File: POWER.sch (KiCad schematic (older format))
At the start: 58 parts

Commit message: update power mark,
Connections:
- net labels added: VCC-IO
- net labels removed: Vcc-io
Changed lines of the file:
@@
 $Descr A3 16535 11693
 encoding utf-8
-Sheet 6 33
+Sheet 6 34
 Title ""
 Date ""
@@
 $EndComp
 $Comp
-L taobao-components:Vcc-io #PWR?
-U 1 1 5C34B9F1
-P 10800 4400
-F 0 "#PWR?" H 10800 4250 50  0001 C CNN
-F 1 "Vcc-io" H 10850 4550 50  0000 C CNN
-F 2 "" H 10800 4400 50  0001 C CNN
-F 3 "" H 10800 4400 50  0001 C CNN
-	1    10800 4400
-	1    0    0    -1
-$EndComp
-$Comp
 L taobao-c:C104,0603 C?
 U 1 1 5C34BB9C
@@
 Wire Wire Line
 	8550 4800 8550 5200
-$Comp
-L taobao-components:Vcc-io #PWR?
-U 1 1 5C39DCD8
-P 8550 6050
-F 0 "#PWR?" H 8550 5900 50  0001 C CNN
-F 1 "Vcc-io" H 8600 6200 50  0000 C CNN
-F 2 "" H 8550 6050 50  0001 C CNN
-F 3 "" H 8550 6050 50  0001 C CNN
-	1    8550 6050
-	1    0    0    -1
-$EndComp
 $Comp
 L taobao-components:AVCC #PWR?
@@
 Wire Wire Line
 	9550 6200 10100 6200
+$Comp
+L taobao-components:VCC-IO #PWR?
+U 1 1 5C7D7758
+P 10800 4400
+F 0 "#PWR?" H 10800 4250 50  0001 C CNN
+F 1 "VCC-IO" H 10850 4550 50  0000 C CNN
+F 2 "" H 10800 4400 50  0001 C CNN
+F 3 "" H 10800 4400 50  0001 C CNN
+	1    10800 4400
+	1    0    0    -1
+$EndComp
+$Comp
+L taobao-components:VCC-IO #PWR?
+U 1 1 5C7D78DC
+P 8550 6050
+F 0 "#PWR?" H 8550 5900 50  0001 C CNN
+F 1 "VCC-IO" H 8600 6200 50  0000 C CNN
+F 2 "" H 8550 6050 50  0001 C CNN
+F 3 "" H 8550 6050 50  0001 C CNN
+	1    8550 6050
+	1    0    0    -1
+$EndComp
 $EndSCHEMATC

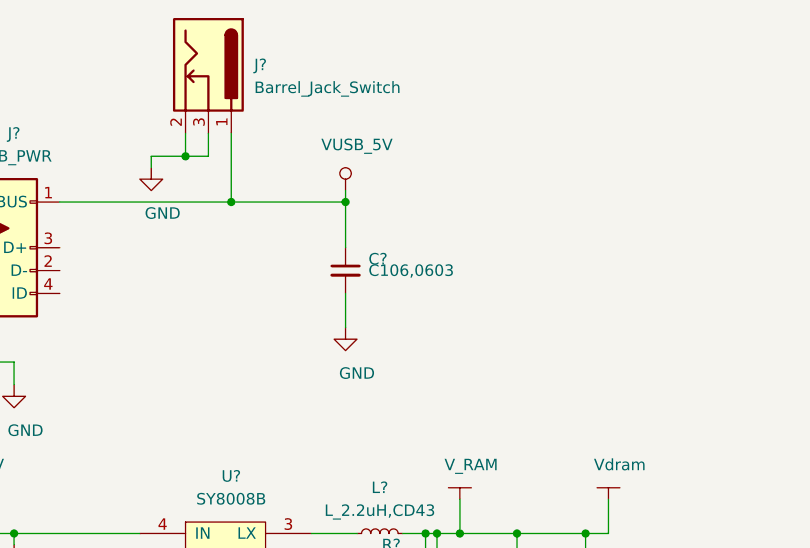
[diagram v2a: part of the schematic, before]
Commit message: add fuse,
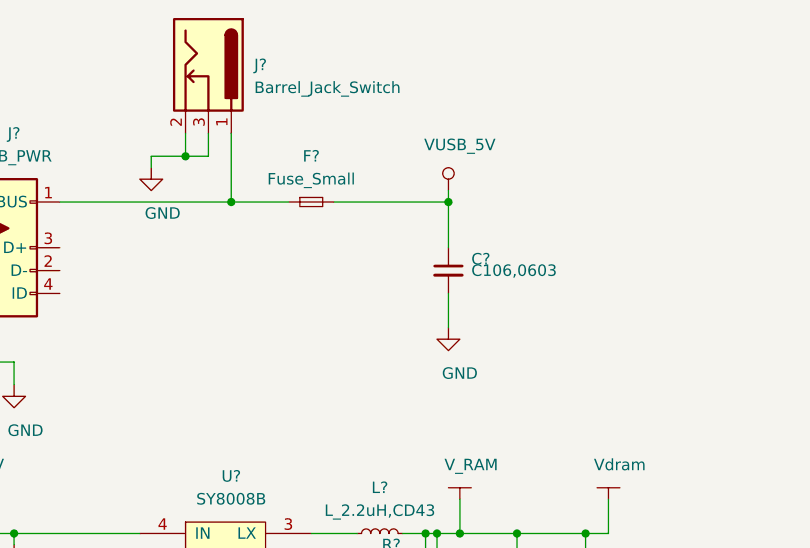
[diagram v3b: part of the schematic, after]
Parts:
- added F?: Fuse_Small, symbol Device:Fuse_Small
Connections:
- net VUSB_5V: now also F?.2; no longer J?.1, J?.1 (VBUS)
- new net: F?.1, J?.1, J?.1 (VBUS)
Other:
- moved on the sheet: C?
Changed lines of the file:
@@
 L taobao-components:VUSB_5V #PWR?
 U 1 1 5C785224
-P 5900 2000
-F 0 "#PWR?" H 5900 1850 50  0001 C CNN
-F 1 "VUSB_5V" H 5950 2200 50  0000 C CNN
-F 2 "" H 5900 2000 50  0001 C CNN
-F 3 "" H 5900 2000 50  0001 C CNN
-	1    5900 2000
+P 6350 2000
+F 0 "#PWR?" H 6350 1850 50  0001 C CNN
+F 1 "VUSB_5V" H 6400 2200 50  0000 C CNN
+F 2 "" H 6350 2000 50  0001 C CNN
+F 3 "" H 6350 2000 50  0001 C CNN
+	1    6350 2000
 	1    0    0    -1
 $EndComp
@@
 L taobao-c:C106,0603 C?
 U 1 1 5C7853BF
-P 5900 2350
-F 0 "C?" H 6000 2400 50  0000 L CNN
-F 1 "C106,0603" H 6000 2350 50  0000 L CNN
-F 2 "Capacitor_SMD:C_0603_1608Metric_Pad1.05x0.95mm_HandSolder" H 5900 2350 50  0001 C CNN
-F 3 "~" H 5900 2350 50  0001 C CNN
-	1    5900 2350
-	1    0    0    -1
-$EndComp
-Wire Wire Line
-	5400 2050 5900 2050
-Wire Wire Line
-	5900 2050 5900 2000
-Connection ~ 5400 2050
-Wire Wire Line
-	5900 2050 5900 2250
-Connection ~ 5900 2050
+P 6350 2350
+F 0 "C?" H 6450 2400 50  0000 L CNN
+F 1 "C106,0603" H 6450 2350 50  0000 L CNN
+F 2 "Capacitor_SMD:C_0603_1608Metric_Pad1.05x0.95mm_HandSolder" H 6350 2350 50  0001 C CNN
+F 3 "~" H 6350 2350 50  0001 C CNN
+	1    6350 2350
+	1    0    0    -1
+$EndComp
+Wire Wire Line
+	6350 2050 6350 2000
+Wire Wire Line
+	6350 2050 6350 2250
+Connection ~ 6350 2050
 $Comp
 L power:GND #PWR?
 U 1 1 5C78561A
-P 5900 2600
-F 0 "#PWR?" H 5900 2350 50  0001 C CNN
-F 1 "GND" H 5950 2400 50  0000 C CNN
-F 2 "" H 5900 2600 50  0001 C CNN
-F 3 "" H 5900 2600 50  0001 C CNN
-	1    5900 2600
-	1    0    0    -1
-$EndComp
-Wire Wire Line
-	5900 2450 5900 2600
+P 6350 2600
+F 0 "#PWR?" H 6350 2350 50  0001 C CNN
+F 1 "GND" H 6400 2400 50  0000 C CNN
+F 2 "" H 6350 2600 50  0001 C CNN
+F 3 "" H 6350 2600 50  0001 C CNN
+	1    6350 2600
+	1    0    0    -1
+$EndComp
+Wire Wire Line
+	6350 2450 6350 2600
 $Comp
 L taobao-components:VUSB_5V #PWR?
@@
 	1    0    0    -1
 $EndComp
+$Comp
+L Device:Fuse_Small F?
+U 1 1 5C37F30E
+P 5750 2050
+F 0 "F?" H 5750 2250 50  0000 C CNN
+F 1 "Fuse_Small" H 5750 2150 50  0000 C CNN
+F 2 "" H 5750 2050 50  0001 C CNN
+F 3 "~" H 5750 2050 50  0001 C CNN
+	1    5750 2050
+	1    0    0    -1
+$EndComp
+Wire Wire Line
+	5650 2050 5400 2050
+Connection ~ 5400 2050
+Wire Wire Line
+	5850 2050 6350 2050
 $EndSCHEMATC

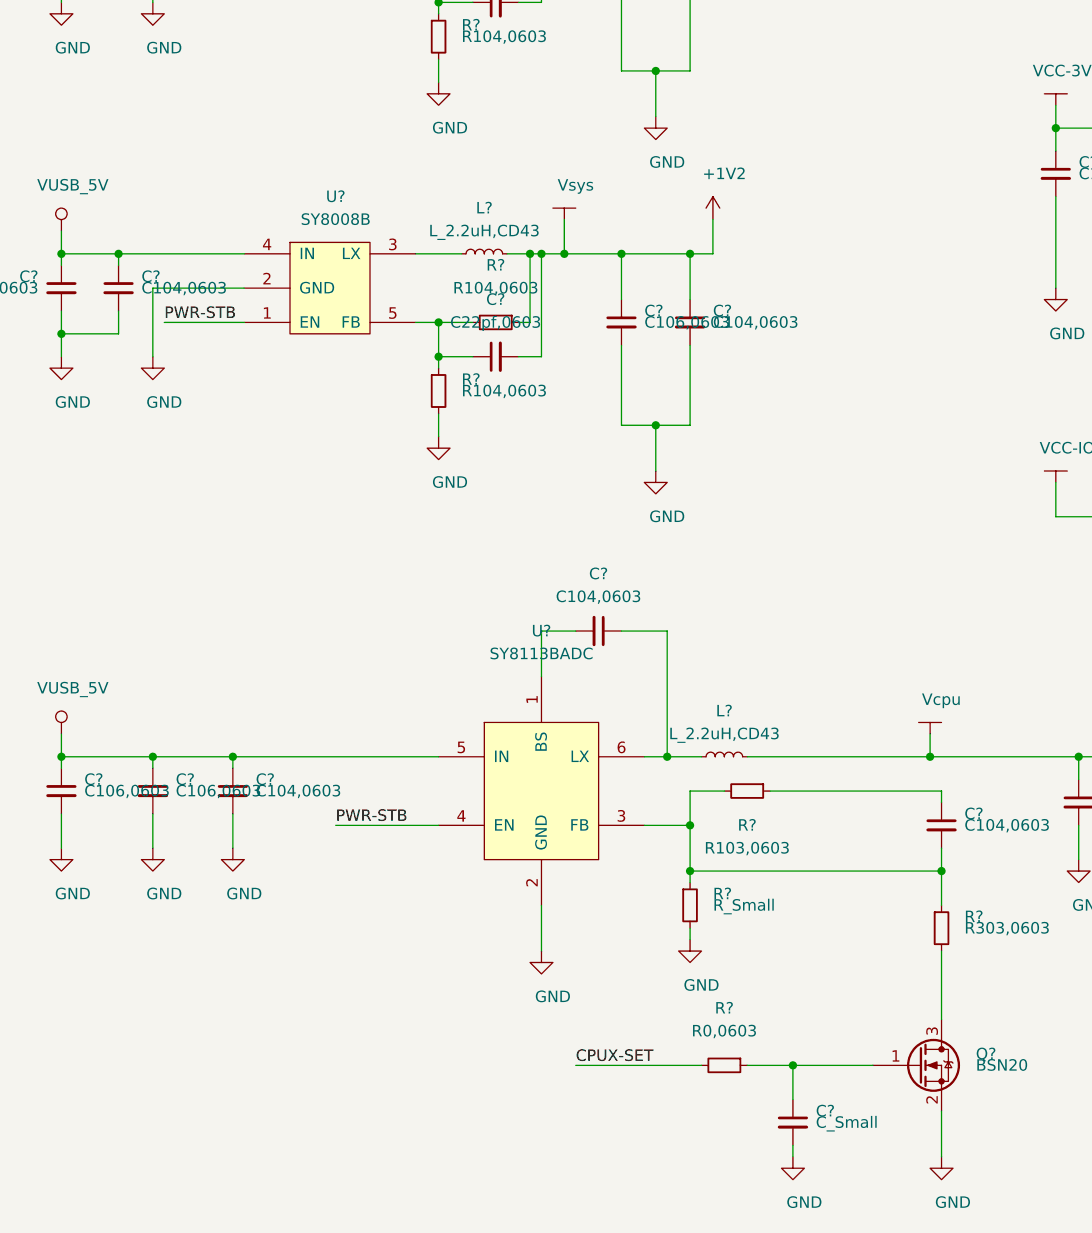
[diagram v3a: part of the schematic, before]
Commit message: update CPU power,
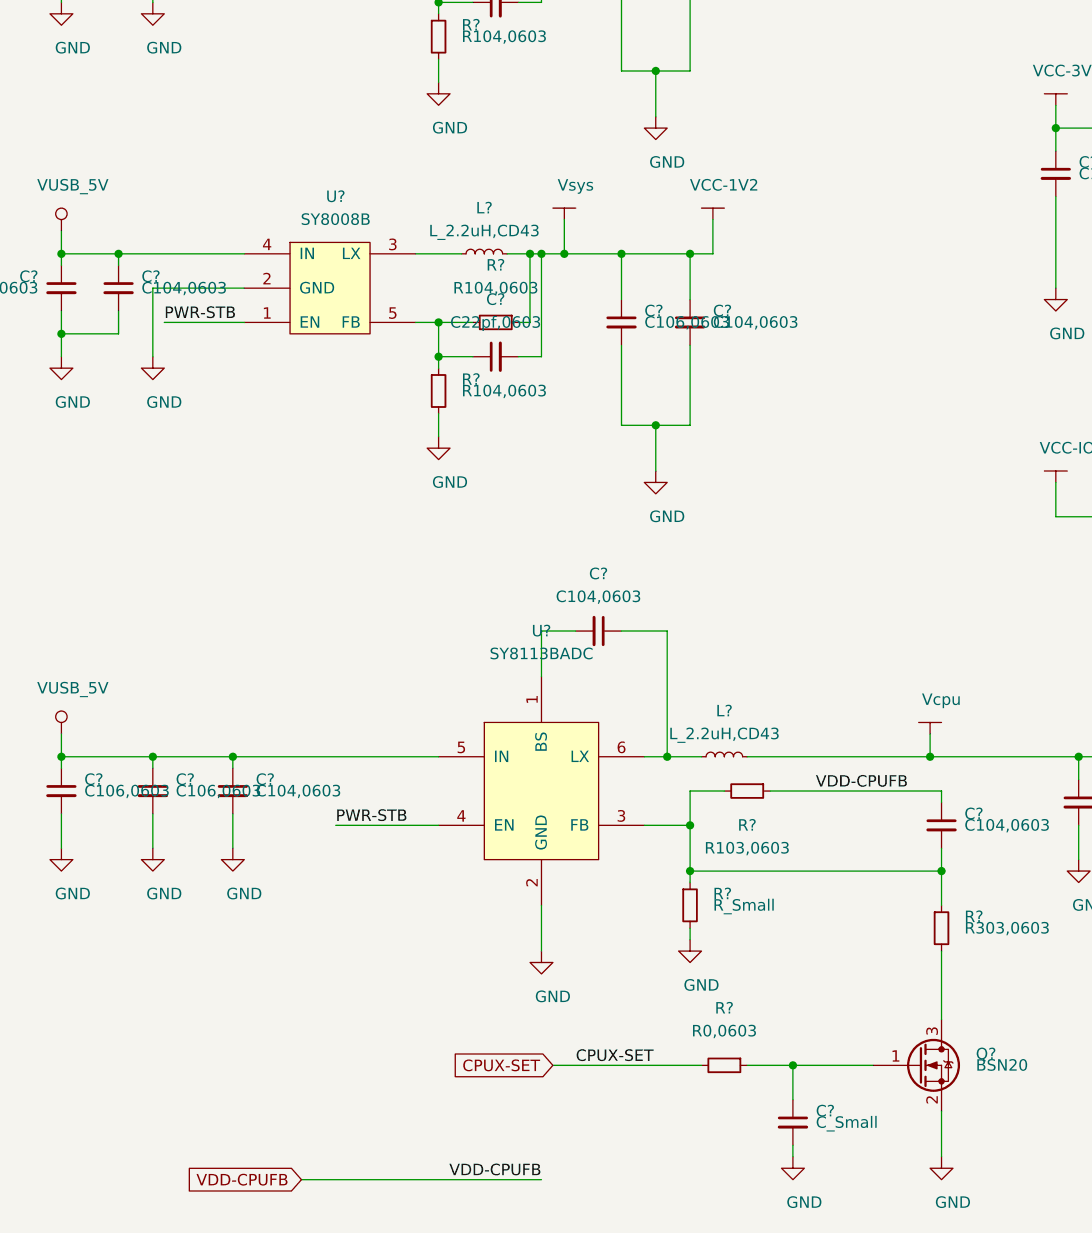
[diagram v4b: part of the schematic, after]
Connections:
- net VDD-CPUFB: now reaches C?.1, R?.1
- net +1V2 renamed VCC-1V2
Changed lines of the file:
@@
-$EndComp
-$Comp
-L power:+1V2 #PWR?
-U 1 1 5C1E907F
-P 7050 4900
-F 0 "#PWR?" H 7050 4750 50  0001 C CNN
-F 1 "+1V2" H 7100 5100 50  0000 C CNN
-F 2 "" H 7050 4900 50  0001 C CNN
-F 3 "" H 7050 4900 50  0001 C CNN
-	1    7050 4900
-	1    0    0    -1
 $EndComp
 $Comp
@@
 Text Label 6450 8600 0    50   ~ 0
 CPUX-SET
-Wire Wire Line
-	6450 8600 7000 8600
 $Comp
 L taobao-components:VUSB_5V #PWR?
@@
 Wire Wire Line
 	5850 2050 6350 2050
+$Comp
+L taobao-components:VCC-1V2 #PWR?
+U 1 1 5C3A3C4D
+P 7050 4900
+F 0 "#PWR?" H 7050 4750 50  0001 C CNN
+F 1 "VCC-1V2" H 7100 5050 50  0000 C CNN
+F 2 "" H 7050 4900 50  0001 C CNN
+F 3 "" H 7050 4900 50  0001 C CNN
+	1    7050 4900
+	1    0    0    -1
+$EndComp
+Text Label 7500 7400 0    50   ~ 0
+VDD-CPUFB
+Text Label 6300 9100 2    50   ~ 0
+VDD-CPUFB
+Text GLabel 5250 9100 0    50   Input ~ 0
+VDD-CPUFB
+Wire Wire Line
+	5250 9100 6300 9100
+Wire Wire Line
+	6350 8600 7000 8600
+Text GLabel 6350 8600 0    50   Input ~ 0
+CPUX-SET
 $EndSCHEMATC

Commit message: update,
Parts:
- removed C?: C104,0603, Capacitor_SMD:C_0603_1608Metric_Pad1.05x0.95mm_HandSolder, symbol taobao-c:C104,0603
- added C?: C_NC,0603, Capacitor_SMD:C_0603_1608Metric_Pad1.05x0.95mm_HandSolder, symbol taobao-components:C_NC,0603
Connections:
- net VDD-CPUFB: now also C?.1
- net at R?.1, R?.1, R?.2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: now also C?.2
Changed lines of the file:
@@
 P 4200 7400
 F 0 "C?" H 4300 7450 50  0000 L CNN
-F 1 "C106,0603" H 4300 7400 50  0000 L CNN
+F 1 "C106,0603" V 4300 7400 50  0000 L CNN
 F 2 "Capacitor_SMD:C_0603_1608Metric_Pad1.05x0.95mm_HandSolder" H 4200 7400 50  0001 C CNN
 F 3 "~" H 4200 7400 50  0001 C CNN
@@
 P 4600 7400
 F 0 "C?" H 4700 7450 50  0000 L CNN
-F 1 "C106,0603" H 4700 7400 50  0000 L CNN
+F 1 "C106,0603" V 4700 7400 50  0000 L CNN
 F 2 "Capacitor_SMD:C_0603_1608Metric_Pad1.05x0.95mm_HandSolder" H 4600 7400 50  0001 C CNN
 F 3 "~" H 4600 7400 50  0001 C CNN
@@
 P 4950 7400
 F 0 "C?" H 5050 7450 50  0000 L CNN
-F 1 "C104,0603" H 5050 7400 50  0000 L CNN
+F 1 "C104,0603" V 5050 7400 50  0000 L CNN
 F 2 "Capacitor_SMD:C_0603_1608Metric_Pad1.05x0.95mm_HandSolder" H 4950 7400 50  0001 C CNN
 F 3 "~" H 4950 7400 50  0001 C CNN
@@
 	6950 7400 6950 7550
 Connection ~ 6950 7550
-$Comp
-L taobao-c:C104,0603 C?
-U 1 1 5C2268D4
-P 8050 7550
-F 0 "C?" H 8150 7600 50  0000 L CNN
-F 1 "C104,0603" H 8150 7550 50  0000 L CNN
-F 2 "Capacitor_SMD:C_0603_1608Metric_Pad1.05x0.95mm_HandSolder" H 8050 7550 50  0001 C CNN
-F 3 "~" H 8050 7550 50  0001 C CNN
-	1    8050 7550
-	1    0    0    -1
-$EndComp
 Wire Wire Line
 	8050 7450 8050 7400
@@
 P 8650 7450
 F 0 "C?" H 8750 7500 50  0000 L CNN
-F 1 "C106,0603" H 8750 7450 50  0000 L CNN
+F 1 "C106,0603" V 8750 7450 50  0000 L CNN
 F 2 "Capacitor_SMD:C_0603_1608Metric_Pad1.05x0.95mm_HandSolder" H 8650 7450 50  0001 C CNN
 F 3 "~" H 8650 7450 50  0001 C CNN
@@
 P 8950 7450
 F 0 "C?" H 9050 7500 50  0000 L CNN
-F 1 "C106,0603" H 9050 7450 50  0000 L CNN
+F 1 "C106,0603" V 9050 7450 50  0000 L CNN
 F 2 "Capacitor_SMD:C_0603_1608Metric_Pad1.05x0.95mm_HandSolder" H 8950 7450 50  0001 C CNN
 F 3 "~" H 8950 7450 50  0001 C CNN
@@
 P 9250 7450
 F 0 "C?" H 9350 7500 50  0000 L CNN
-F 1 "C104,0603" H 9350 7450 50  0000 L CNN
+F 1 "C104,0603" V 9350 7450 50  0000 L CNN
 F 2 "Capacitor_SMD:C_0603_1608Metric_Pad1.05x0.95mm_HandSolder" H 9250 7450 50  0001 C CNN
 F 3 "~" H 9250 7450 50  0001 C CNN
@@
 P 9600 7450
 F 0 "C?" H 9700 7500 50  0000 L CNN
-F 1 "TC107,16V" H 9700 7450 50  0000 L CNN
+F 1 "TC107,16V" V 9700 7450 50  0000 L CNN
 F 2 "" H 9600 7450 50  0001 C CNN
 F 3 "~" H 9600 7450 50  0001 C CNN
@@
 Text GLabel 6350 8600 0    50   Input ~ 0
 CPUX-SET
+$Comp
+L taobao-components:C_NC,0603 C?
+U 1 1 5C3D1DE4
+P 8050 7550
+F 0 "C?" H 8150 7600 50  0000 L CNN
+F 1 "C_NC,0603" H 8150 7550 50  0000 L CNN
+F 2 "Capacitor_SMD:C_0603_1608Metric_Pad1.05x0.95mm_HandSolder" H 8050 7550 50  0001 C CNN
+F 3 "~" H 8050 7550 50  0001 C CNN
+	1    8050 7550
+	1    0    0    -1
+$EndComp
 $EndSCHEMATC

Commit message: update,
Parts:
- removed C?: C_Small, symbol Device:C_Small
- added C?: C_NC,0603, Capacitor_SMD:C_0603_1608Metric_Pad1.05x0.95mm_HandSolder, symbol taobao-components:C_NC,0603
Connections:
- net GND: now also C?.2
- net at Q?.1 (G), R?.1: now also C?.1
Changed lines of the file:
@@
 	8050 8100 8050 8400
-$Comp
-L Device:C_Small C?
-U 1 1 5C28EE49
-P 7400 8850
-F 0 "C?" H 7500 8900 50  0000 L CNN
-F 1 "C_Small" H 7500 8850 50  0000 L CNN
-F 2 "" H 7400 8850 50  0001 C CNN
-F 3 "~" H 7400 8850 50  0001 C CNN
-	1    7400 8850
-	1    0    0    -1
-$EndComp
 $Comp
 L power:GND #PWR?
@@
 	1    0    0    -1
 $EndComp
+$Comp
+L taobao-components:C_NC,0603 C?
+U 1 1 5C3D84B0
+P 7400 8850
+F 0 "C?" H 7500 8900 50  0000 L CNN
+F 1 "C_NC,0603" H 7500 8850 50  0000 L CNN
+F 2 "Capacitor_SMD:C_0603_1608Metric_Pad1.05x0.95mm_HandSolder" H 7400 8850 50  0001 C CNN
+F 3 "~" H 7400 8850 50  0001 C CNN
+	1    7400 8850
+	1    0    0    -1
+$EndComp
